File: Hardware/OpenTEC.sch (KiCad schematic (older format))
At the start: 68 parts, among them J10 TEMP3, J11 TEC, J12 XH2.54, J13 XH2.54, J14 XH2.54, J15 XH2.54, J16 XH2.54, J17 XH2.54, J18 XH2.54, J19 XH2.54, J2 4P Screw Terminal, J20 XH2.54, J21 XH2.54, J22 XH2.54, J3 10P JTAG/SWD, J4 LCD, J5 I2C, J6 BOOT_SEL, J7 TEMP0, J8 TEMP1, J9 TEMP2, Q1 IRL2703, Q2 IRL2703, Q3 IRL2703, Q4 IRL2703, SW1 SW_Left, SW2 SW_Mid, SW3 SW_Right, U1 STM32F103C8T6, U2 AMS1117-3.3, U3 IR2104, U4 IR2104, Y1 16MHz

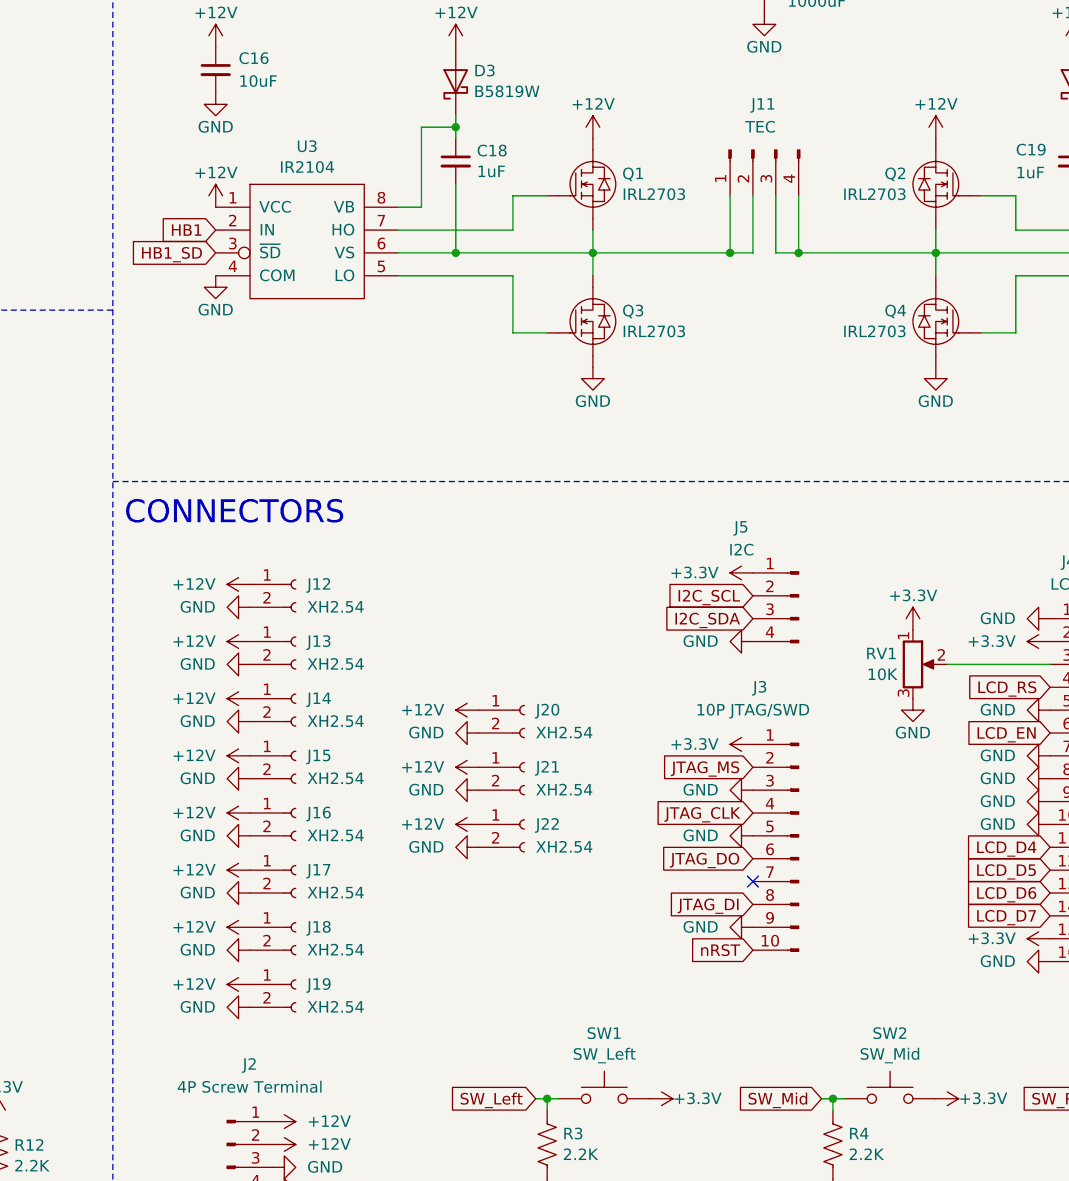
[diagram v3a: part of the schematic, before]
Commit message: Add more vias to H-bridge
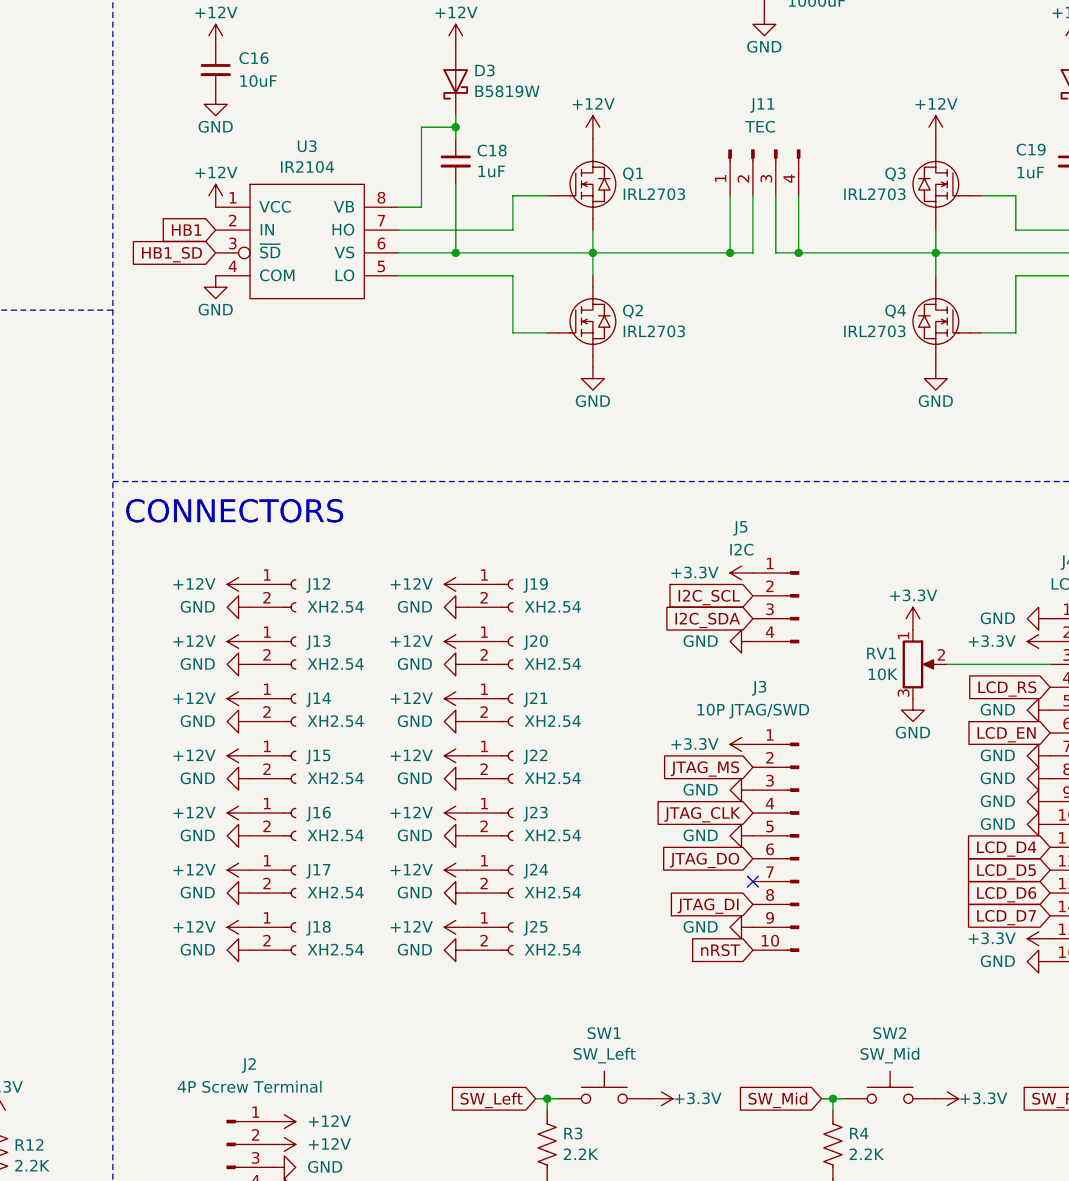
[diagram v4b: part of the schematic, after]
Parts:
- added J23, J24, J25: XH2.54, Connector_JST:JST_XH_B2B-XH-A_1x02_P2.50mm_Vertical, symbol Connector:Conn_01x02_Female
- renumbered Q3 to Q2, Q2 to Q3
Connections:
- net +12V: now also J23.1 (Pin_1), J24.1 (Pin_1), J25.1 (Pin_1)
- net GND: now also J23.2 (Pin_2), J24.2 (Pin_2), J25.2 (Pin_2)
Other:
- moved on the sheet: J19, J20, J21
